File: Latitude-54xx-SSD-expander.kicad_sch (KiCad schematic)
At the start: 24 parts, among them J1 Bus_M.2_Socket_M, J2 Bus_M.2_Socket_M, J3 Bus_M.2_Socket_M, J4 qwiic, U1 clockbuffer_9ZXL0651AKLF

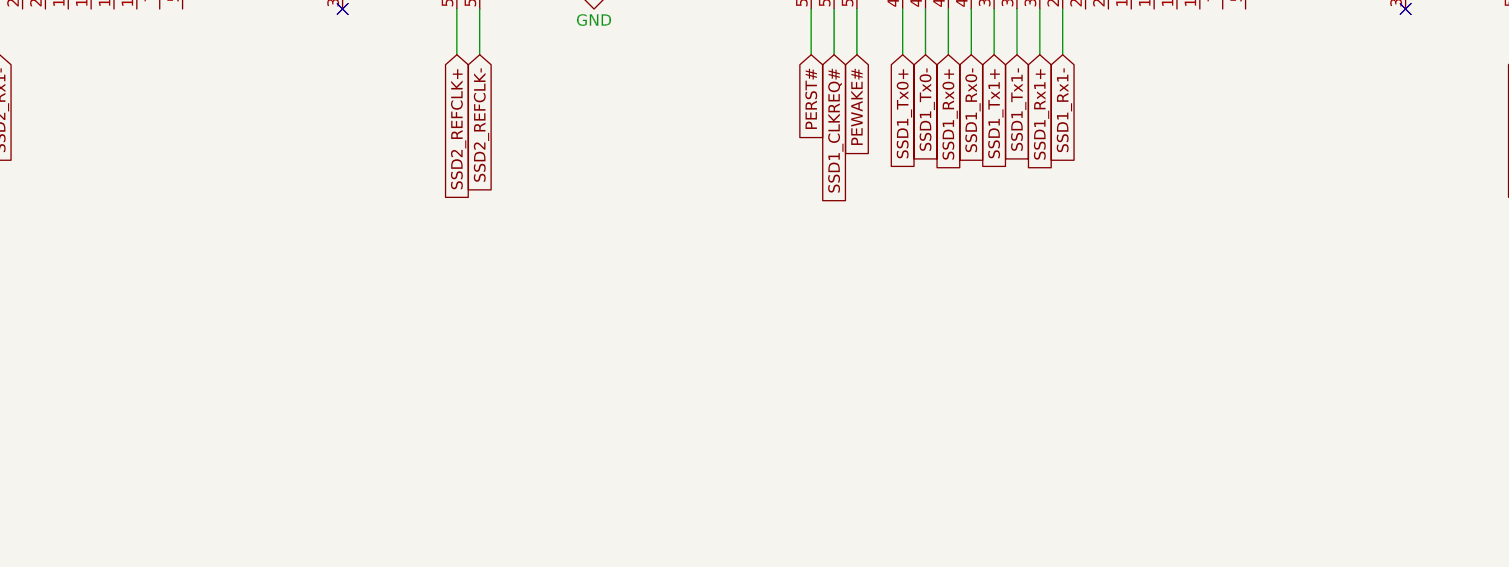
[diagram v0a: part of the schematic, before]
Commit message: Added capacitors for m.2 slots and ground vias for pcie
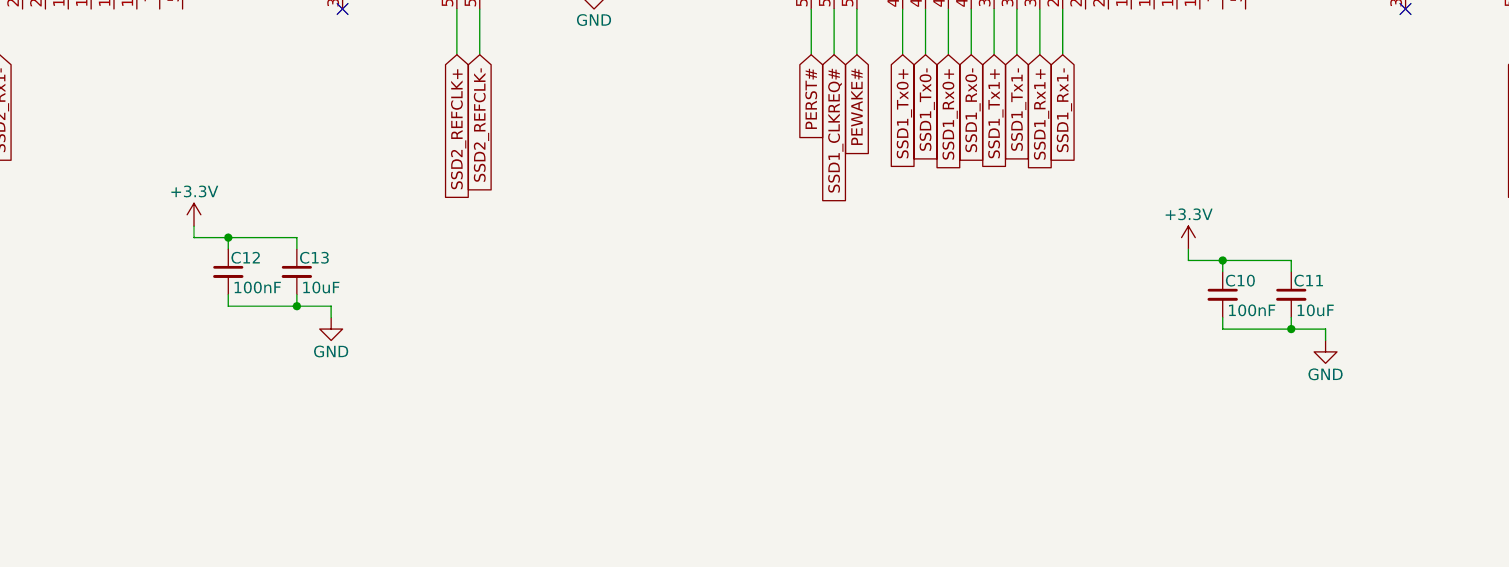
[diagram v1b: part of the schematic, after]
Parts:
- added C10, C12: 100nF, Capacitor_SMD:C_0603_1608Metric, symbol Device:C_Small
- added C11, C13: 10uF, Capacitor_SMD:C_0603_1608Metric, symbol Device:C_Small
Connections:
- net +3.3V: now also C10.1, C11.1, C12.1, C13.1
- net GND: now also C10.2, C11.2, C12.2, C13.2

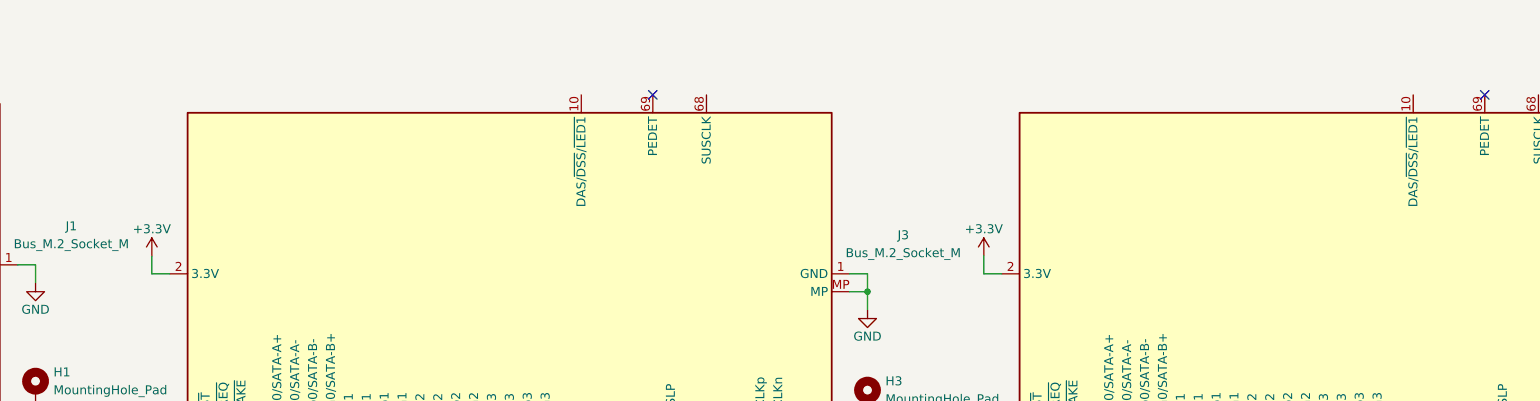
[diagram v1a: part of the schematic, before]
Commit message: Added activity leds
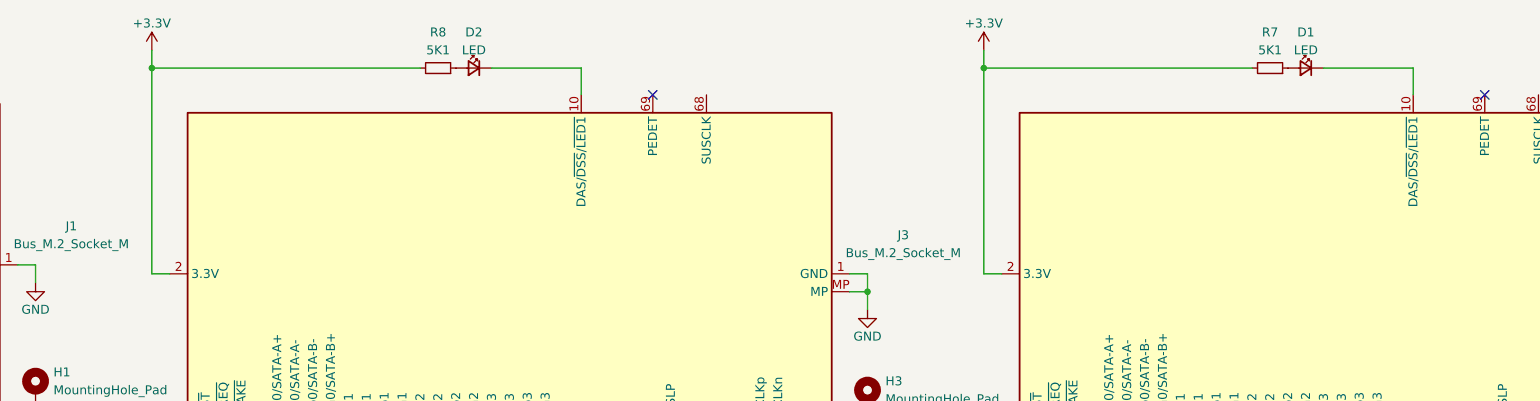
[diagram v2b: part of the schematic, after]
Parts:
- added D1, D2: LED, Diode_SMD:D_0603_1608Metric, symbol Device:LED_Small
- added R7, R8: 5K1, Resistor_SMD:R_0603_1608Metric, symbol Device:R_Small
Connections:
- net +3.3V: now also R7.2, R8.2
- net at J3.10 (DAS/~{DSS}/~{LED1}): now also D2.1 (K)
- net at J2.10 (DAS/~{DSS}/~{LED1}): now also D1.1 (K)
- new net: D2.2 (A), R8.1
- new net: D1.2 (A), R7.1

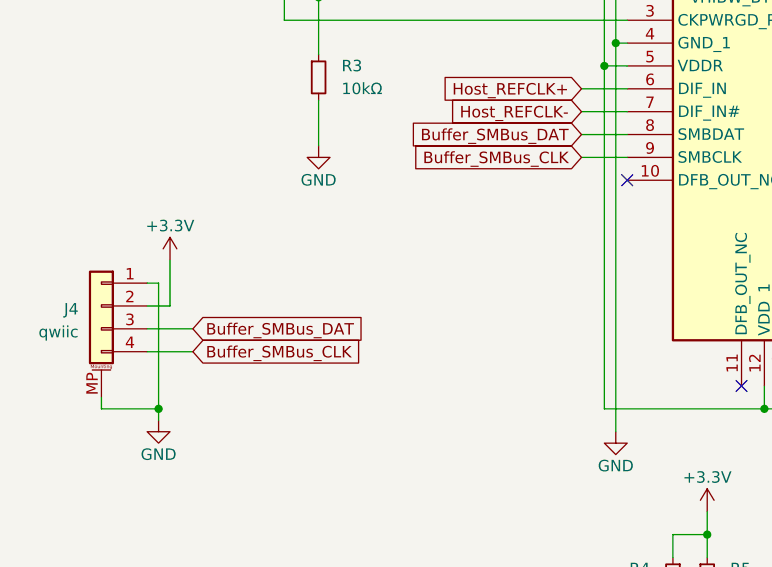
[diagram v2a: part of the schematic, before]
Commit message: Added i2c pullups
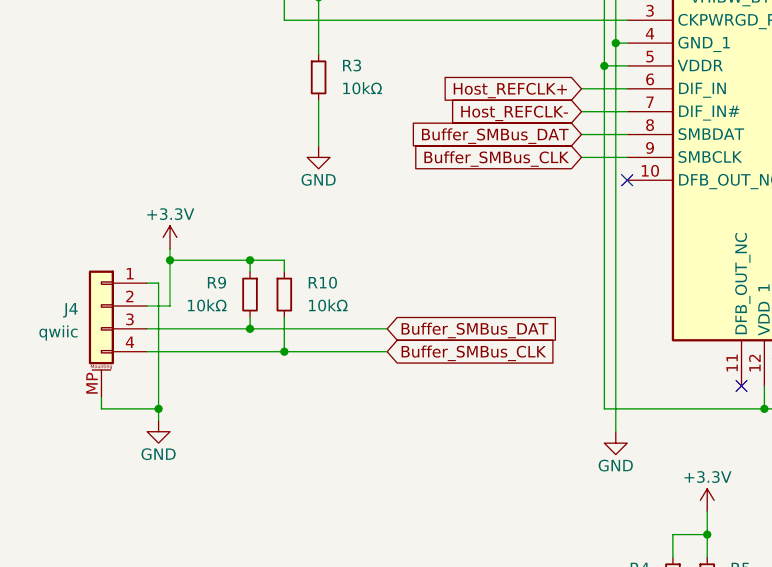
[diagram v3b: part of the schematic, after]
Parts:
- added R10, R9: 10kΩ, Resistor_SMD:R_0603_1608Metric, symbol Device:R_Small
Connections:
- net +3.3V: now also R10.1, R9.1
- net Buffer_SMBus_CLK: now also R10.2
- net Buffer_SMBus_DAT: now also R9.2

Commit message: page note
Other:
- company: (none) -> WifiCable
- title: (none) -> Latitude 5491 SSD Expander
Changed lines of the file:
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@@
 	(generator_version "8.0")
 	(paper "A3")
+	(title_block
+		(title "Latitude 5491 SSD Expander")
+		(company "WifiCable")
+	)
 	(junction
 		(at 106.68 137.16)

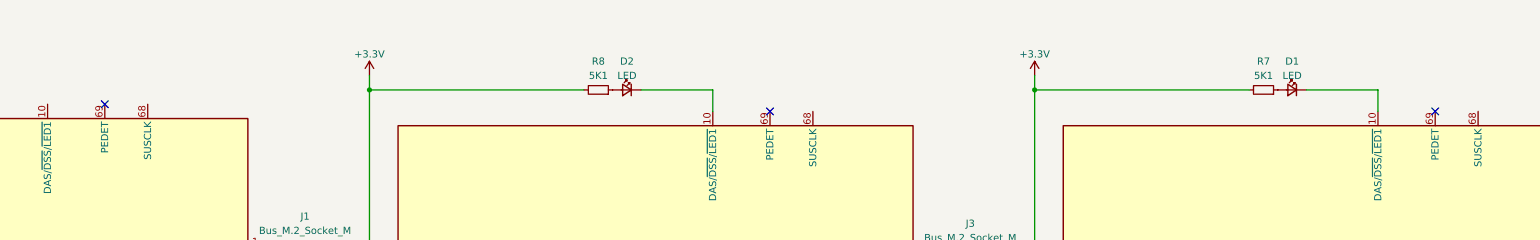
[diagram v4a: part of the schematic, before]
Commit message: Connected PEDET for first slot
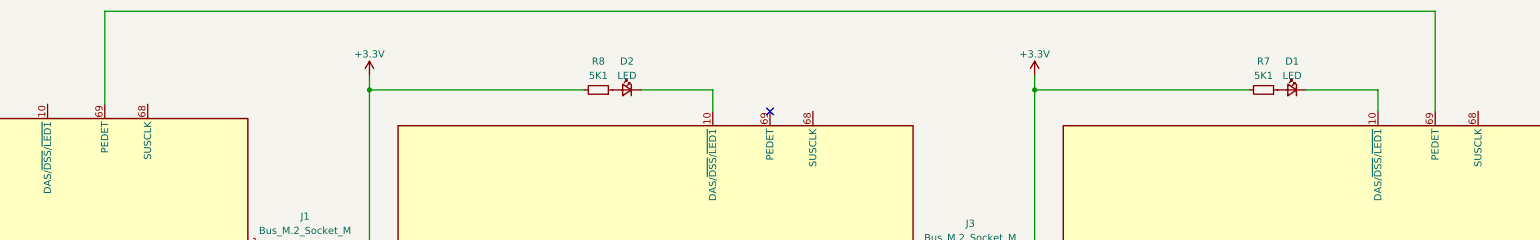
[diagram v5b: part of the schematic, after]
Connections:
- net at J1.69 (PEDET): now also J2.69 (PEDET)
- no-connect marks 10 -> 8
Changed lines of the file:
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@@
-	)
-	(no_connect
-		(at 339.09 36.83)
 	)
 	(no_connect
@@
 		(at 220.98 36.83)
 	)
-	(no_connect
-		(at 102.87 35.56)
-	)
 	(wire
 		(pts
@@
 	(wire
 		(pts
+			(xy 102.87 19.05) (xy 102.87 35.56)
+		)
+		(stroke
+			(width 0)
+			(type default)
+		)
+	)
+	(wire
+		(pts
 			(xy 114.3 134.62) (xy 134.62 134.62)
 		)
@@
 	(wire
 		(pts
+			(xy 339.09 36.83) (xy 339.09 19.05)
+		)
+		(stroke
+			(width 0)
+			(type default)
+		)
+	)
+	(wire
+		(pts
 			(xy 170.18 189.23) (xy 177.8 189.23)
 		)
@@
 		)
 		(stroke
+			(width 0)
+			(type default)
+		)
+	)
+	(wire
+		(pts
+			(xy 339.09 19.05) (xy 102.87 19.05)
+		)
+		(stroke

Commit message: v2
replaced buffer with 9DBL411BGLFT, fixed impedance (for JLC), added spare refclk breakouts, added ssd smbus breakout, added host activity LED option, improved PCIe pair layout. todo: fix standoff footprints
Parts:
- removed C4, C5, C6, C7, C8, C9: 100nF, Capacitor_SMD:C_0603_1608Metric, symbol Device:C_Small
- removed H4: MountingHole_Pad, TestPoint:TestPoint_THTPad_D3.0mm_Drill1.5mm, symbol Mechanical:MountingHole_Pad
- removed J2, J3: Bus_M.2_Socket_M, A_my_stuff:m-key, symbol Connector:Bus_M.2_Socket_M
- removed R1, R10, R2, R3, R9: 10kΩ, Resistor_SMD:R_0603_1608Metric, symbol Device:R_Small
- removed U1: clockbuffer_9ZXL0651AKLF, A-my-stuff:clockbuffer_9ZXL0651AKLF, symbol A-my-stuff:clockbuffer_9ZXL0651AKLF
- added J2, J3: M-key-full, A-my-stuff:m-key, symbol A-my-stuff:M-key-full
- added J5, J6: refqwock, Connector_JST:JST_SH_SM04B-SRSS-TB_1x04-1MP_P1.00mm_Horizontal, symbol Connector_Generic_MountingPin:Conn_01x04_MountingPin
- added J7: qwiic, Connector_JST:JST_SH_SM04B-SRSS-TB_1x04-1MP_P1.00mm_Horizontal, symbol Connector_Generic_MountingPin:Conn_01x04_MountingPin
- added JP1: SSD1_ledjumper, Resistor_SMD:R_0402_1005Metric, symbol Jumper:SolderJumper_2_Open
- added JP2: SSD2_ledjumper, Resistor_SMD:R_0402_1005Metric, symbol Jumper:SolderJumper_2_Open
- added R4: 10kΩ, Resistor_SMD:R_0603_1608Metric, symbol Device:R_Small
- added TP1: smalert, TestPoint:TestPoint_Pad_D1.0mm, symbol Connector:TestPoint
- added U2: clockbuffer_RENESAS_9DBL411BGLFT, A-my-stuff:clockbuffer_RENESAS 9DBL411BGLFT, symbol A-my-stuff:clockbuffer_RENESAS_9DBL411BGLFT
- renumbered R4 to R1, R5 to R2, R6 to R3, R7 to R5, R8 to R6
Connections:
- net +3.3V: now also J2.12 (3.3V), J2.14 (3.3V), J2.16 (3.3V), J2.18 (3.3V), J2.2 (3.3V), J2.4 (3.3V), J2.70 (3.3V), J2.72 (3.3V), J2.74 (3.3V), J3.12 (3.3V), J3.14 (3.3V), J3.16 (3.3V), J3.18 (3.3V), J3.2 (3.3V), J3.4 (3.3V), J3.70 (3.3V), J3.72 (3.3V), J3.74 (3.3V), R4.1, U2.18 (VDD_IO), U2.4 (VDDA), U2.9 (VDD_IO)
- net GND: now also J2.1 (GND), J2.15 (GND), J2.21 (GND), J2.27 (GND), J2.3 (GND), J2.33 (GND), J2.39 (GND), J2.45 (GND), J2.51 (GND), J2.57 (GND), J2.71 (GND), J2.73 (GND), J2.75 (GND), J2.9 (GND), J2.MP, J3.1 (GND), J3.15 (GND), J3.21 (GND), J3.27 (GND), J3.3 (GND), J3.33 (GND), J3.39 (GND), J3.45 (GND), J3.51 (GND), J3.57 (GND), J3.71 (GND), J3.73 (GND), J3.75 (GND), J3.9 (GND), J3.MP, J5.1 (Pin_1), J5.MP (MountPin), J6.1 (Pin_1), J6.MP (MountPin), J7.1 (Pin_1), J7.MP (MountPin), U2.10 (GND), U2.17 (GND), U2.5 (GNDA)
- net Host_REFCLK+: now also U2.2 (CLK_IN-)
- net Host_REFCLK-: now also U2.3 (CLK_IN+)
- net PERST#: now also J2.50 (~{PERST}), J3.50 (~{PERST})
- net PEWAKE#: now also J2.54 (~{PEWAKE}), J3.54 (~{PEWAKE})
- net SSD1_CLKREQ#: now also J2.52 (~{CLKREQ}), U2.1 (~{OE0})
- net SSD1_REFCLK+: now also J2.55 (REFCLKp), U2.19 (CLK_OUT0-)
- net SSD1_REFCLK-: now also J2.53 (REFCLKn), U2.20 (CLK_OUT0+)
- net SSD1_Rx0+: now also J2.43 (PERp0/SATA-B-)
- net SSD1_Rx0-: now also J2.41 (PERn0/SATA-B+)
- net SSD1_Rx1+: now also J2.31 (PERp1)
- net SSD1_Rx1-: now also J2.29 (PERn1)
- net SSD1_Tx0+: now also J2.49 (PETp0/SATA-A+)
- net SSD1_Tx0-: now also J2.47 (PETn0/SATA-A-)
- net SSD1_Tx1+: now also J2.37 (PETp1)
- net SSD1_Tx1-: now also J2.35 (PETn1)
- net SSD2_CLKREQ#: now also J3.52 (~{CLKREQ}), U2.16 (~{OE1})
- net SSD2_REFCLK+: now also J3.55 (REFCLKp), U2.14 (CLK_OUT1-)
- net SSD2_REFCLK-: now also J3.53 (REFCLKn), U2.15 (CLK_OUT1+)
- net SSD2_Rx0+: now also J3.43 (PERp0/SATA-B-)
- net SSD2_Rx0-: now also J3.41 (PERn0/SATA-B+)
- net SSD2_Rx1+: now also J3.31 (PERp1)
- net SSD2_Rx1-: now also J3.29 (PERn1)
- net SSD2_Tx0+: now also J3.49 (PETp0/SATA-A+)
- net SSD2_Tx0-: now also J3.47 (PETn0/SATA-A-)
- net SSD2_Tx1+: now also J3.37 (PETp1)
- net SSD2_Tx1-: now also J3.35 (PETn1)
- net SSD2_LED#: now reaches D2.1 (K)
- net SSD2_LED#: now also J3.10 (DAS/~{DSS}/~{LED1}), JP2.2 (B)
- net at J1.10 (DAS/~{DSS}/~{LED1}): now also JP1.1 (A), JP2.1 (A)
- net SSD1_PEDET#: now reaches J1.69 (PEDET)
- net SSD1_PEDET#: now also J2.69 (PEDET)
- net CLKREQ3#: now reaches R3.2
- net CLKREQ3#: now also J5.2 (Pin_2), U2.13 (~{OE2})
- net SSD1_LED#: now reaches D1.1 (K)
- net SSD1_LED#: now also J2.10 (DAS/~{DSS}/~{LED1}), JP1.2 (B)
- net Buffer_SMBus_CLK renamed SSD2_SMCLK
- net SSD2_SMCLK: now also J3.40 (NC/SMBus_CLK)
- net Buffer_SMBus_DAT renamed SSD2_SMDAT
- net SSD2_SMDAT: now also J3.42 (NC/SMBus_DAT)
- new net CLKREQ4#: J6.2 (Pin_2), R4.2, U2.6 (~{OE3})
- new net REFCLK3+: J5.4 (Pin_4), U2.11 (CLK_OUT2-)
- new net REFCLK3-: J5.3 (Pin_3), U2.12 (CLK_OUT2+)
- new net REFCLK4+: J6.4 (Pin_4), U2.7 (CLK_OUT3-)
- new net REFCLK4-: J6.3 (Pin_3), U2.8 (CLK_OUT3+)
- new net SSD2_SMALERT#: J3.44 (NC/ALERT#), TP1.1
- no-connect marks 8 -> 1
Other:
- moved on the sheet: C1, C10, C11, C12, C13, C2, C3, D1, D2, H2, H3, J4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

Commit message: fixed m.2 standoff footprints, v2 done?
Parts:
- H2, H3: footprint MountingHole:MountingHole_3.5mm_Pad -> MountingHole:MountingHole_4mm_Pad
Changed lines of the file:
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@@
 			)
 		)
-		(property "Footprint" "MountingHole:MountingHole_3.5mm_Pad"
+		(property "Footprint" "MountingHole:MountingHole_4mm_Pad"
 			(at 243.84 72.39 0)
 			(effects
@@
 			)
 		)
-		(property "Footprint" "MountingHole:MountingHole_3.5mm_Pad"
+		(property "Footprint" "MountingHole:MountingHole_4mm_Pad"
 			(at 367.03 72.39 0)
 			(effects

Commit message: changed led jumpers to custom solderjumpers
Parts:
- JP1, JP2: footprint Resistor_SMD:R_0402_1005Metric -> A-my-stuff:mySolderJumper-1x0.5mm
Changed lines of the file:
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@@
 			)
 		)
-		(property "Footprint" "Resistor_SMD:R_0402_1005Metric"
+		(property "Footprint" "A-my-stuff:mySolderJumper-1x0.5mm"
 			(at 91.44 26.67 0)
 			(effects
@@
 			)
 		)
-		(property "Footprint" "Resistor_SMD:R_0402_1005Metric"
+		(property "Footprint" "A-my-stuff:mySolderJumper-1x0.5mm"
 			(at 93.98 26.67 0)
 			(effects
